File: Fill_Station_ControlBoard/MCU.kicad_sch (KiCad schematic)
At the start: 47 parts, among them J4 Conn_02x05_Counter_Clockwise, SW1 CK_KMS2xxG, SW2 BOOT, U1 STM32H747IITx, Y1 Crystal 25MHz, Y2 Crystal 32.768 kHz

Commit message: début layout
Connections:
- net NJTRST is gone; now on net NJRST: U1.163 (PB4)
- net Servo.Signal1: now reaches U1.67 (PE7)
- net Servo.Signal2: now reaches U1.68 (PE8)
- net Servo.Signal3: now reaches U1.69 (PE9)
- no-connect marks 83 -> 80
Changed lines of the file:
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@@
-	)
-	(no_connect
-		(at 142.24 207.01)
 	)
 	(no_connect
@@
 	)
 	(no_connect
-		(at 142.24 209.55)
-	)
-	(no_connect
 		(at 142.24 199.39)
 	)
@@
 	(no_connect
 		(at 238.76 217.17)
-	)
-	(no_connect
-		(at 142.24 204.47)
 	)
 	(no_connect
@@
 		)
 	)
+	(label "JTDO"
+		(at 238.76 105.41 0)
+		(effects
+			(font
+				(size 1.27 1.27)
+			)
+			(justify left bottom)
+		)
+	)
 	(label "VDD5_USB"
 		(at 201.93 19.05 0)
@@
 			)
 			(justify right bottom)
+		)
+	)
+	(label "NJRST"
+		(at 238.76 107.95 0)
+		(effects
+			(font
+				(size 1.27 1.27)
+			)
+			(justify left bottom)
+		)
+	)
+	(hierarchical_label "Servo.Signal2"
+		(shape input)
+		(at 142.24 207.01 180)
+		(effects
+			(font
+				(size 1.27 1.27)
+			)
+			(justify right)
 		)
 	)
@@
 		)
 	)
+	(hierarchical_label "Servo.Signal1"
+		(shape input)
+		(at 142.24 204.47 180)
+		(effects
+			(font
+				(size 1.27 1.27)
+			)
+			(justify right)
+		)
+	)
 	(hierarchical_label "Eth.MDIO"
 		(shape bidirectional)
@@
 		)
 	)
-	(hierarchical_label "JTDO"
-		(shape input)
-		(at 238.76 105.41 0)
-		(effects
-			(font
-				(size 1.27 1.27)
-			)
-			(justify left)
-		)
-	)
 	(hierarchical_label "GPIO4"
 		(shape input)
@@
 		)
 	)
+	(hierarchical_label "Servo.Signal3"
+		(shape input)
+		(at 142.24 209.55 180)
+		(effects
+			(font
+				(size 1.27 1.27)
+			)
+			(justify right)
+		)
+	)
 	(hierarchical_label "SD.DAT3"
 		(shape input)
@@
 		(effects
 			(font
-				(size 1.27 1.27)
-			)
-			(justify left)
-		)
-	)
-	(hierarchical_label "NJTRST"
-		(shape input)
-		(at 238.76 107.95 0)
-		(effects
-			(font

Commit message: Ajout power
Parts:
- removed Y1: Crystal 25MHz, Crystal:Crystal_SMD_3225-4Pin_3.2x2.5mm, symbol Device:Crystal
- removed Y2: Crystal 32.768 kHz, Crystal:Crystal_SMD_3225-4Pin_3.2x2.5mm, symbol Device:Crystal
- added C49, C50: 1u, Capacitor_SMD:C_0603_1608Metric, symbol Device:C
- added C6, C7: 100n, Capacitor_SMD:C_0402_1005Metric, symbol Device:C
- added R38, R48: 10k, Resistor_SMD:R_0603_1608Metric_Pad0.98x0.95mm_HandSolder, symbol Device:R_US
- added R47: 0, Resistor_SMD:R_0603_1608Metric_Pad0.98x0.95mm_HandSolder, symbol Device:R_US
- added Y1: ASV-32.768kHz, Oscillator:Oscillator_SMD_Abracon_ASV-4Pin_7.0x5.1mm, symbol Oscillator:ASV-xxxMHz
- added Y3: ASV-25.000MHz, Oscillator:Oscillator_SMD_Abracon_ASV-4Pin_7.0x5.1mm, symbol Oscillator:ASV-xxxMHz
- C26: value 6pF -> 10u; footprint Capacitor_SMD:C_0603_1608Metric -> Capacitor_SMD:C_0402_1005Metric
- C27: value 6pF -> *; footprint Capacitor_SMD:C_0603_1608Metric -> Capacitor_SMD:C_0402_1005Metric; now not fitted
- C33: value * -> 100n; footprint Capacitor_SMD:C_0603_1608Metric -> Capacitor_SMD:C_0402_1005Metric
- C34: value * -> 10u; footprint Capacitor_SMD:C_0603_1608Metric -> Capacitor_SMD:C_0402_1005Metric
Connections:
- net JTMS is gone; now on net SWDIO: J4.10 (Pin_10)
- net 3V3: now also C26.1, C33.1, C34.1, C49.1, C50.1, C7.1, R38.1, R48.1, Y1.4 (Vdd), Y3.4 (Vdd)
- net CAN.RXD: now also U1.168 (PB8); no longer U1.169 (PB9)
- net CAN.TXD: now also U1.169 (PB9); no longer U1.168 (PB8)
- net Eth.TXD0: now also U1.85 (PB12); no longer U1.157 (PG13)
- net GND: now also C26.2, C27.2, SW1.SH (B), C49.2, C50.2, C6.2, C7.2, Y1.2 (GND), Y3.2 (GND); no longer C1.2, C19.2, C20.2, C21.2, C22.2, C26.1, C27.1, C36.2, C55.2, C56.2, C57.2
- net Clock_32.768khz: now reaches U1.10 (PC14)
- net Clock_32.768khz: now also Y1.3 (OUT); no longer C33.1
- net at U1.11 (PC15): no longer C34.1
- net Clock_25Mhz: now reaches U1.31 (PH0)
- net Clock_25Mhz: now also C27.1, R47.2; no longer C26.2
- net SWDIO: now reaches U1.132 (PA13)
- net CAN.FAULT: now reaches U1.170 (PE0)
- net LED1: now reaches U1.3 (PE4)
- net at U1.32 (PH1): no longer C27.2
- net NRST: now reaches R27.2, SW1.2, U1.33 (NRST)
- net NRST: now also J4.6 (Pin_6), C6.1
- net LED2: now reaches U1.4 (PE5)
- net LED3: now reaches U1.5 (PE6)
- net CAN.STBY: no longer names the net of U1.146 (PD3)
- net Eth.RXER: no longer names the net of U1.110 (PG2)
- net JTCK renamed SWCLK
- net JTDI: no longer names the net of J4.7 (Pin_7)
- net JTDI: no longer U1.139 (PA15)
- net JTDO renamed SWO
- net NJRST: no longer names the net of U1.163 (PB4)
- net NJRST: no longer J4.6 (Pin_6)
- net VDD5_USB renamed 5V
- new net: C1.2, C19.2, C20.2, C21.2, C22.2, C36.2, C55.2, C56.2, C57.2
- new net: R38.2, Y3.1 (EN)
- new net: R47.1, Y3.3 (OUT)
- new net: R48.2, Y1.1 (EN)
- no-connect marks 80 -> 82
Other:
- note added: "BOOT"
- note added: "DECOUPLING MCU"
- note added: "EXTERNAL OSCILLATOR"
- note added: "Microchip Pinout"
- note added: "RESET"
- note added: "SWD"
- note removed: "Laisser flotante?"
- moved on the sheet: C1, C11, C14, C15, C16, C17, C18, C19, C2, C20, C21, C22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

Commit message: début layout
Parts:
- J12: renamed from J4; footprint (none) -> Connector_PinSocket_2.00mm:PinSocket_2x05_P2.00mm_Vertical
- R52: renamed from R38; footprint Resistor_SMD:R_0603_1608Metric_Pad0.98x0.95mm_HandSolder -> Capacitor_SMD:C_0402_1005Metric
- R54: renamed from R47; footprint Resistor_SMD:R_0603_1608Metric_Pad0.98x0.95mm_HandSolder -> Capacitor_SMD:C_0402_1005Metric
- renumbered C6 to C15, C48 to C16, C31 to C17, C25 to C18, C24 to C19, C32 to C20, C23 to C21, C42 to C22, C43 to C23, C44 to C24, C55 to C25, C2 to C26, C3 to C27, C56 to C28, C4 to C29, C1 to C30, C5 to C31, C19 to C32, C8 to C33, C20 to C34, C14 to C35, C57 to C36, C15 to C37, C21 to C38, C16 to C39, C22 to C40, C17 to C41, C36 to C42, C18 to C43, C54 to C44, C50 to C45, C7 to C46, C49 to C47, C33 to C48, C26 to C49, C11 to C50, C27 to C51, C34 to C52, C40 to C53, C41 to C54, R27 to R49, R14 to R50, R39 to R51, R48 to R53, U1 to U2, Y3 to Y1, Y1 to Y2
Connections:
- net Clock_25Mhz renamed Clock25Mhz

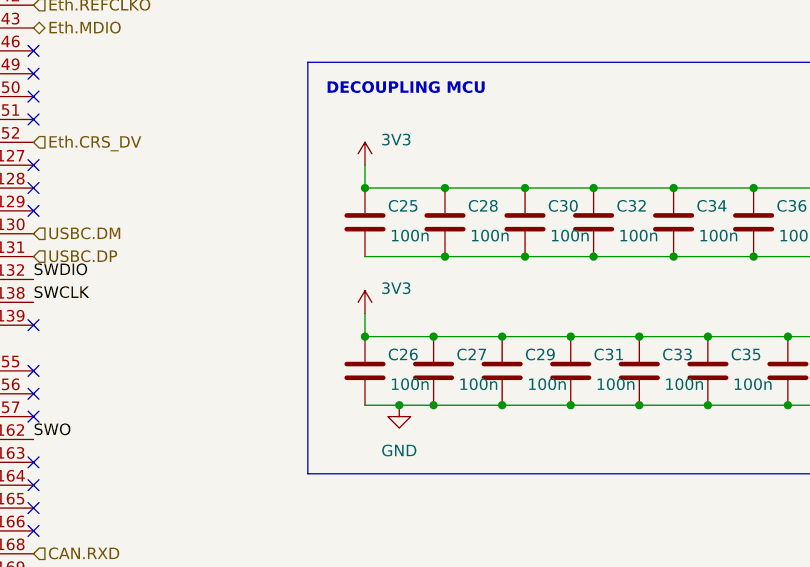
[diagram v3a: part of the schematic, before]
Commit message: wiring de certaines parties du PCB et placement de quelques composantes sur le PCB
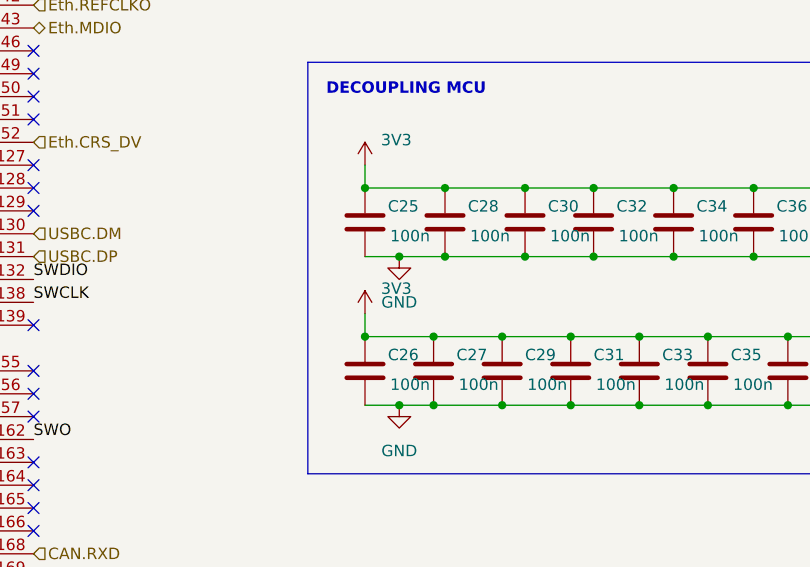
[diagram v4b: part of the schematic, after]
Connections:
- net GND: now also C25.2, C28.2, C30.2, C32.2, C34.2, C36.2, C38.2, C40.2, C42.2
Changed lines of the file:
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@@
 	)
 	(junction
+		(at 279.4 85.09)
+		(diameter 0)
+		(color 0 0 0 0)
+	)
+	(junction
 		(at 306.07 101.6)
 		(diameter 0)
@@
 	(wire
 		(pts
-			(xy 275.59 85.09) (xy 284.48 85.09)
+			(xy 275.59 85.09) (xy 279.4 85.09)
 		)
 		(stroke
@@
 	(wire
 		(pts
+			(xy 279.4 85.09) (xy 284.48 85.09)
+		)
+		(stroke
+			(width 0)
+			(type default)
+		)
+	)
+	(wire
+		(pts
 			(xy 309.88 77.47) (xy 318.77 77.47)
 		)
@@
 					(unit 1)
 				)
+			)
+		)
+	)
+	(symbol
+		(lib_id "power:GND")
+		(at 279.4 85.09 0)
+		(unit 1)
+		(exclude_from_sim no)
+		(in_bom yes)
+		(on_board yes)
+		(dnp no)
+		(fields_autoplaced yes)
+		(property "Reference" "#PWR0132"
+			(at 279.4 91.44 0)
+			(effects
+				(font
+					(size 1.27 1.27)
+				)
+				(hide yes)
+			)
+		)
+		(property "Value" "GND"
+			(at 279.4 90.17 0)
+			(effects
+				(font
+					(size 1.27 1.27)
+				)
+			)
+		)
+		(property "Footprint" ""
+			(at 279.4 85.09 0)
+			(effects
+				(font
+					(size 1.27 1.27)
+				)
+				(hide yes)
+			)
+		)
+		(property "Datasheet" ""
+			(at 279.4 85.09 0)
+			(effects
+				(font
+					(size 1.27 1.27)
+				)
+				(hide yes)
+			)
+		)
+		(property "Description" "Power symbol creates a global label with name \"GND\" , ground"
+			(at 279.4 85.09 0)
+			(effects
+				(font
+					(size 1.27 1.27)
+				)
+				(hide yes)
+			)
+		)
+		(pin "1"
+		)
+		(instances
+			(project "Fill_Station_ControlBoard"
+				(path "/eaacffe0-ee57-428e-a37e-5655e0922ccc/e0f29092-a5b7-4c06-8bb6-3f29401186b8"
+					(reference "#PWR0132")
+					(unit 1)
+				)

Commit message: PCB fait
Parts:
- removed C15, C32: 100n, Capacitor_SMD:C_0402_1005Metric, symbol Device:C
- removed C38: 100n, Capacitor_SMD:C_0603_1608Metric_Pad1.08x0.95mm_HandSolder, symbol Device:C
- removed SW1: CK_KMS2xxG, Button_Switch_SMD:SW_SPST_CK_KMS2xxGP, symbol Switch:CK_KMS2xxG
- added C83: 100n, Capacitor_SMD:C_0402_1005Metric, symbol Device:C
- added C87: 10u, Capacitor_SMD:C_0603_1608Metric, symbol Device:C
- added C88: 100u, Capacitor_SMD:C_0603_1608Metric, symbol Device:C
- added H1, H2, H3, H4: M3_Hole_With_Spacer_H10mm, PCM_SL_Mechanical:MountingHole_3.2mm_With_Spacer_H10mm, symbol PCM_SL_Mechanical:M3_Hole_With_Spacer_H10mm
- added R89: 22, Resistor_SMD:R_0402_1005Metric, symbol Device:R_US
- added SW1: RESET, Button_Switch_SMD:SW_DPDT_CK_JS202011JCQN, symbol Switch:SW_Push_SPDT
- C16, C40: footprint Capacitor_SMD:C_0603_1608Metric_Pad1.08x0.95mm_HandSolder -> Capacitor_SMD:C_0402_1005Metric
- C23, C42: footprint Capacitor_SMD:C_0603_1608Metric -> Capacitor_SMD:C_0402_1005Metric
- L2: footprint (none) -> Resistor_SMD:R_0402_1005Metric
- R49: value 100k -> 10k
- SW2: footprint (none) -> Button_Switch_SMD:SW_DPDT_CK_JS202011JCQN
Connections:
- net 3V3: now also C87.1, C88.1, SW1.3 (C); no longer R49.1
- net 3V3A: now also C83.1
- net CAN.TXD: now also R89.2; no longer U2.169 (PB9)
- net GND: now also C83.2, C87.2, C88.2, H1.1, H2.1, H3.1, H4.1, SW1.1 (A)
- net LED1: now also U2.146 (PD3); no longer U2.3 (PE4)
- net LED2: now also U2.147 (PD4); no longer U2.4 (PE5)
- net LED3: now also U2.148 (PD5); no longer U2.5 (PE6)
- net SWO: no longer U2.162 (PB3)
- net SD2.CLK: now reaches U2.149 (PD6)
- net SD2.DAT3: now reaches U2.163 (PB4)
- net Heater1: now reaches U2.2 (PE3)
- net SD2.CMD: now reaches U2.41 (PA0)
- net SD2.DAT0: now reaches U2.87 (PB14)
- net SD2.DAT1: now reaches U2.88 (PB15)
- net E-Match1_Cont: now reaches U2.89 (PD8)
- net E-Match2_Cont: now reaches U2.90 (PD9)
- net E-Match2_Det: now reaches U2.95 (PD12)
- net E-Match2: now reaches U2.96 (PD13)
- net E-Match1_Det: now reaches U2.97 (PD14)
- net E-Match1: now reaches U2.98 (PD15)
- net SD.CLK renamed SD1.CLK
- net SD.CMD renamed SD1.CMD
- net SD.DAT0 renamed SD1.DAT0
- net SD.DAT1 renamed SD1.DAT1
- net SD.DAT2 renamed SD1.DAT2
- net SD.DAT3 renamed SD1.DAT3
- new net: R49.1, SW1.2 (B)
- new net: R89.1, U2.169 (PB9)
- new net Heater2: U2.3 (PE4)
- new net Heater3: U2.4 (PE5)
- new net SD2.DAT2: U2.162 (PB3)
- no-connect marks 82 -> 68
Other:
- note added: "Mechanical"
- note added: "Plastic stand-off"
- note added: "Short?"
- moved on the sheet: C25, C26, C27, C28, C29, C30, C31, C33, C34, C35, C36, C37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

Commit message: Travail Layout
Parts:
- added C90, C91: 100n, Capacitor_SMD:C_0402_1005Metric, symbol Device:C
- added R103, R113, R114: 22, Resistor_SMD:R_0402_1005Metric, symbol Device:R_US
- R53: footprint Resistor_SMD:R_0603_1608Metric_Pad0.98x0.95mm_HandSolder -> Capacitor_SMD:C_0402_1005Metric
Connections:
- net Eth.RST: now also U2.51 (PA6); no longer U2.1 (PE2)
- net Eth.TXEN: now also R103.2; no longer U2.155 (PG11)
- net GND: now also C90.2, C91.2
- net SD2.CMD: now also U2.150 (PD7); no longer U2.41 (PA0)
- net at R49.1, SW1.2 (B): now also C91.1
- net at R50.1, SW2.2 (B): now also C90.1
- net at U2.79 (PB11): now also R103.1
- net CAN.FAULT: no longer names the net of U2.170 (PE0)
- net Clock25Mhz renamed Clock_25Mhz
- net Eth.RXD0 renamed Eth.RXD_P
- net Eth.RXD1 renamed Eth.RXD_N
- net Eth.TXD0: no longer names the net of U2.85 (PB12)
- net Eth.TXD0: now also R113.1
- net Eth.TXD1: no longer names the net of U2.86 (PB13)
- net Eth.TXD1: now also R114.1
- net SWO: no longer names the net of J12.8 (Pin_8)
- new net Eth.TXD_N: R114.2
- new net Eth.TXD_P: R113.2
- no-connect marks 68 -> 70
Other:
- note added: "Solder"
- note removed: "Short?"

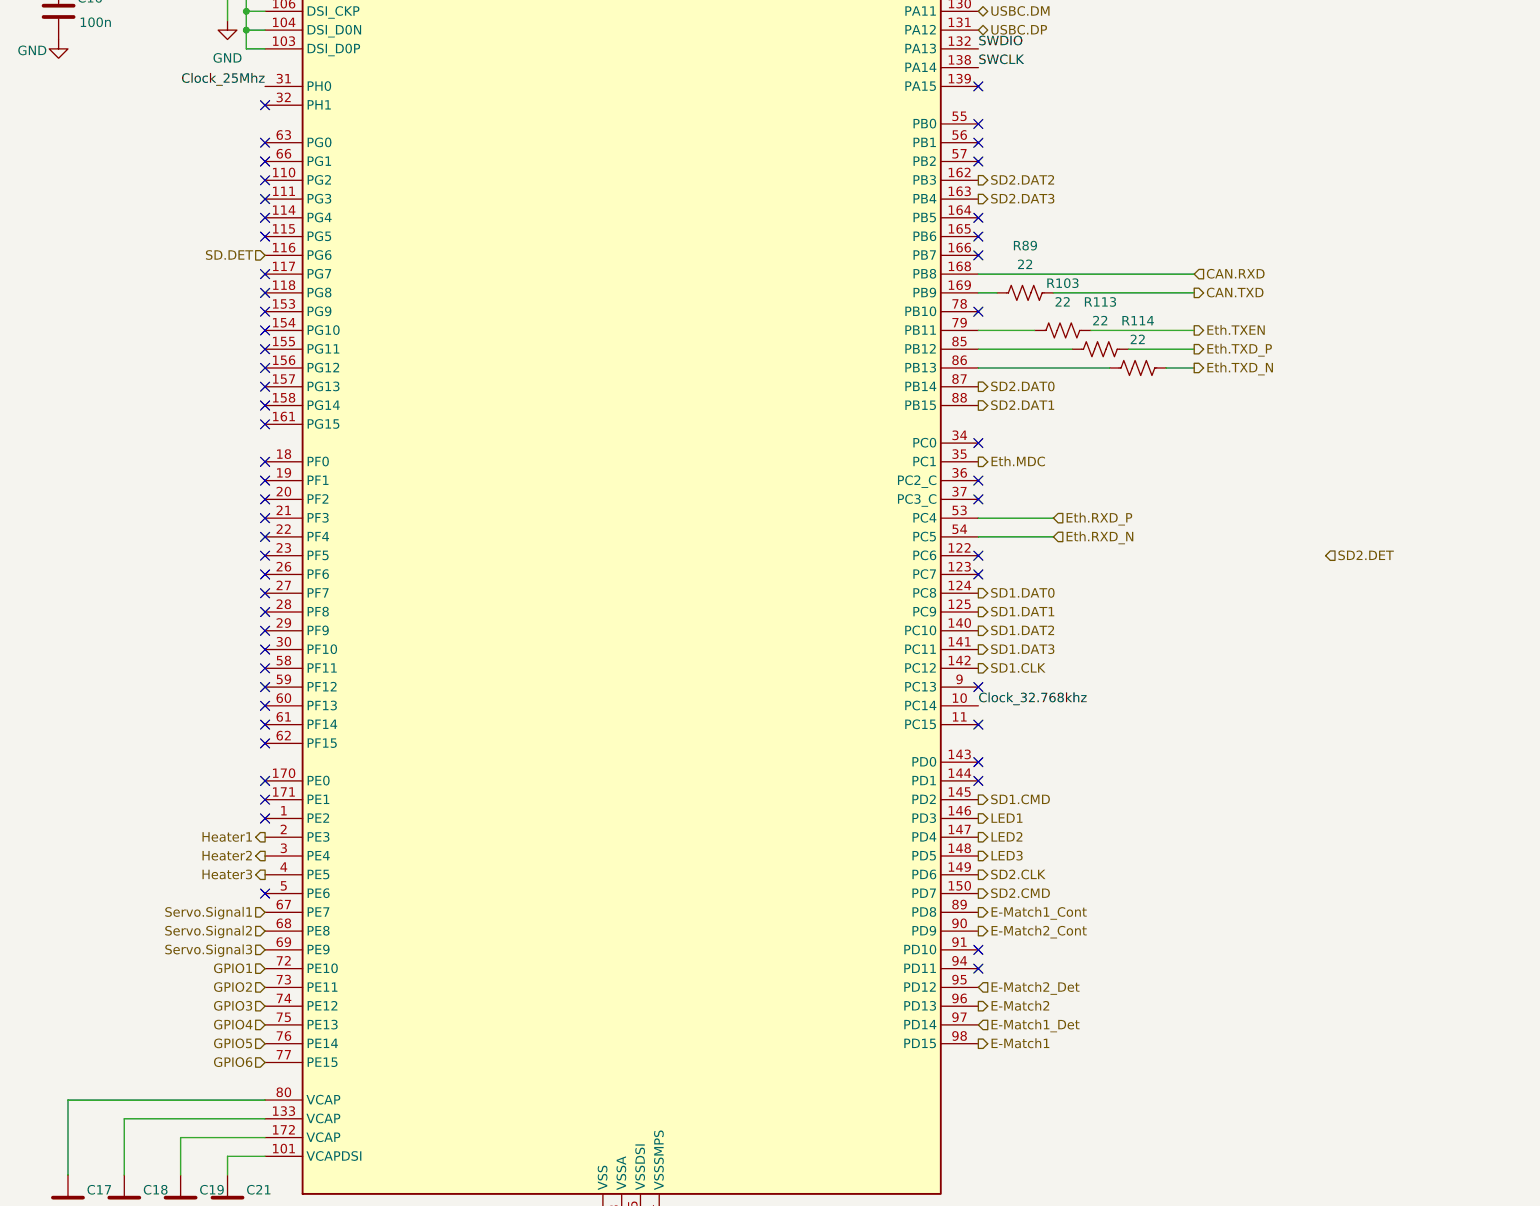
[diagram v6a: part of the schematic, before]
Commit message: PCB presque terminé
Modifs de l'alim
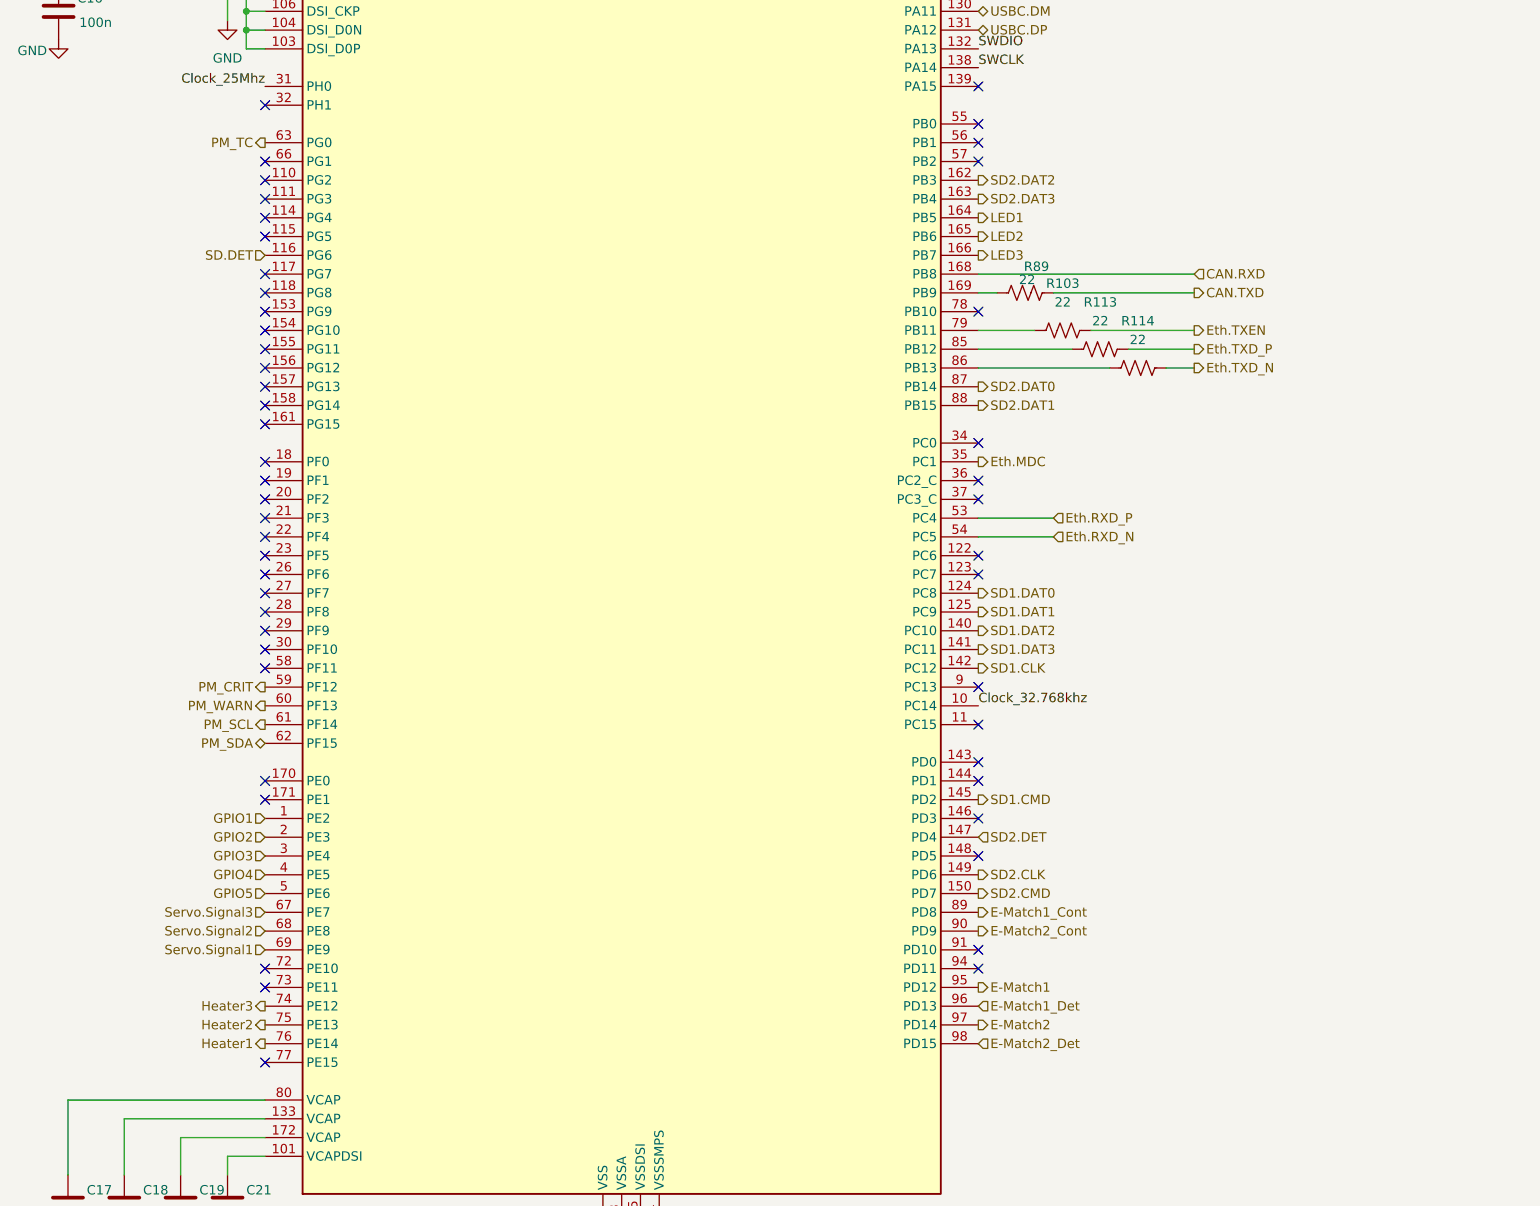
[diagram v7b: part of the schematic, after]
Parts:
- BT1: footprint 0CSL_D1_V1:BatteryHolder_BHX1_1025 -> Battery:Battery_Panasonic_CR2032-HFN_Horizontal_CircularHoles
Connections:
- net E-Match1: now also U2.95 (PD12); no longer U2.98 (PD15)
- net E-Match1_Det: now also U2.96 (PD13); no longer U2.97 (PD14)
- net E-Match2: now also U2.97 (PD14); no longer U2.96 (PD13)
- net E-Match2_Det: now also U2.98 (PD15); no longer U2.95 (PD12)
- net GPIO1: now also U2.1 (PE2); no longer U2.72 (PE10)
- net GPIO2: now also U2.2 (PE3); no longer U2.73 (PE11)
- net GPIO3: now also U2.3 (PE4); no longer U2.74 (PE12)
- net GPIO4: now also U2.4 (PE5); no longer U2.75 (PE13)
- net GPIO5: now also U2.5 (PE6); no longer U2.76 (PE14)
- net Heater1: now also U2.76 (PE14); no longer U2.2 (PE3)
- net Heater2: now also U2.75 (PE13); no longer U2.3 (PE4)
- net Heater3: now also U2.74 (PE12); no longer U2.4 (PE5)
- net LED1: now also U2.164 (PB5); no longer U2.146 (PD3)
- net LED2: now also U2.165 (PB6); no longer U2.147 (PD4)
- net LED3: now also U2.166 (PB7); no longer U2.148 (PD5)
- net SD2.DET: now also U2.147 (PD4)
- net Servo.Signal1: now also U2.69 (PE9); no longer U2.67 (PE7)
- net Servo.Signal3: now also U2.67 (PE7); no longer U2.69 (PE9)
- net PM_CRIT: now reaches U2.59 (PF12)
- net PM_WARN: now reaches U2.60 (PF13)
- net PM_SCL: now reaches U2.61 (PF14)
- net PM_SDA: now reaches U2.62 (PF15)
- net PM_TC: now reaches U2.63 (PG0)
- net GPIO6: no longer names the net of U2.77 (PE15)
- no-connect marks 70 -> 65
